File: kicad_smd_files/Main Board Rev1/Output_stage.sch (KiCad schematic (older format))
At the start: 41 parts, among them J10 OUTPUT B, J9 OUTPUT A, Q3 DMN10H170SK3-13, Q4 DMP6180SK3-13, Q5 DMN10H170SK3-13, Q6 DMN10H170SK3-13, Q7 DMP6180SK3-13, Q8 DMN10H170SK3-13, U7 LM358N, U8 LTC1661

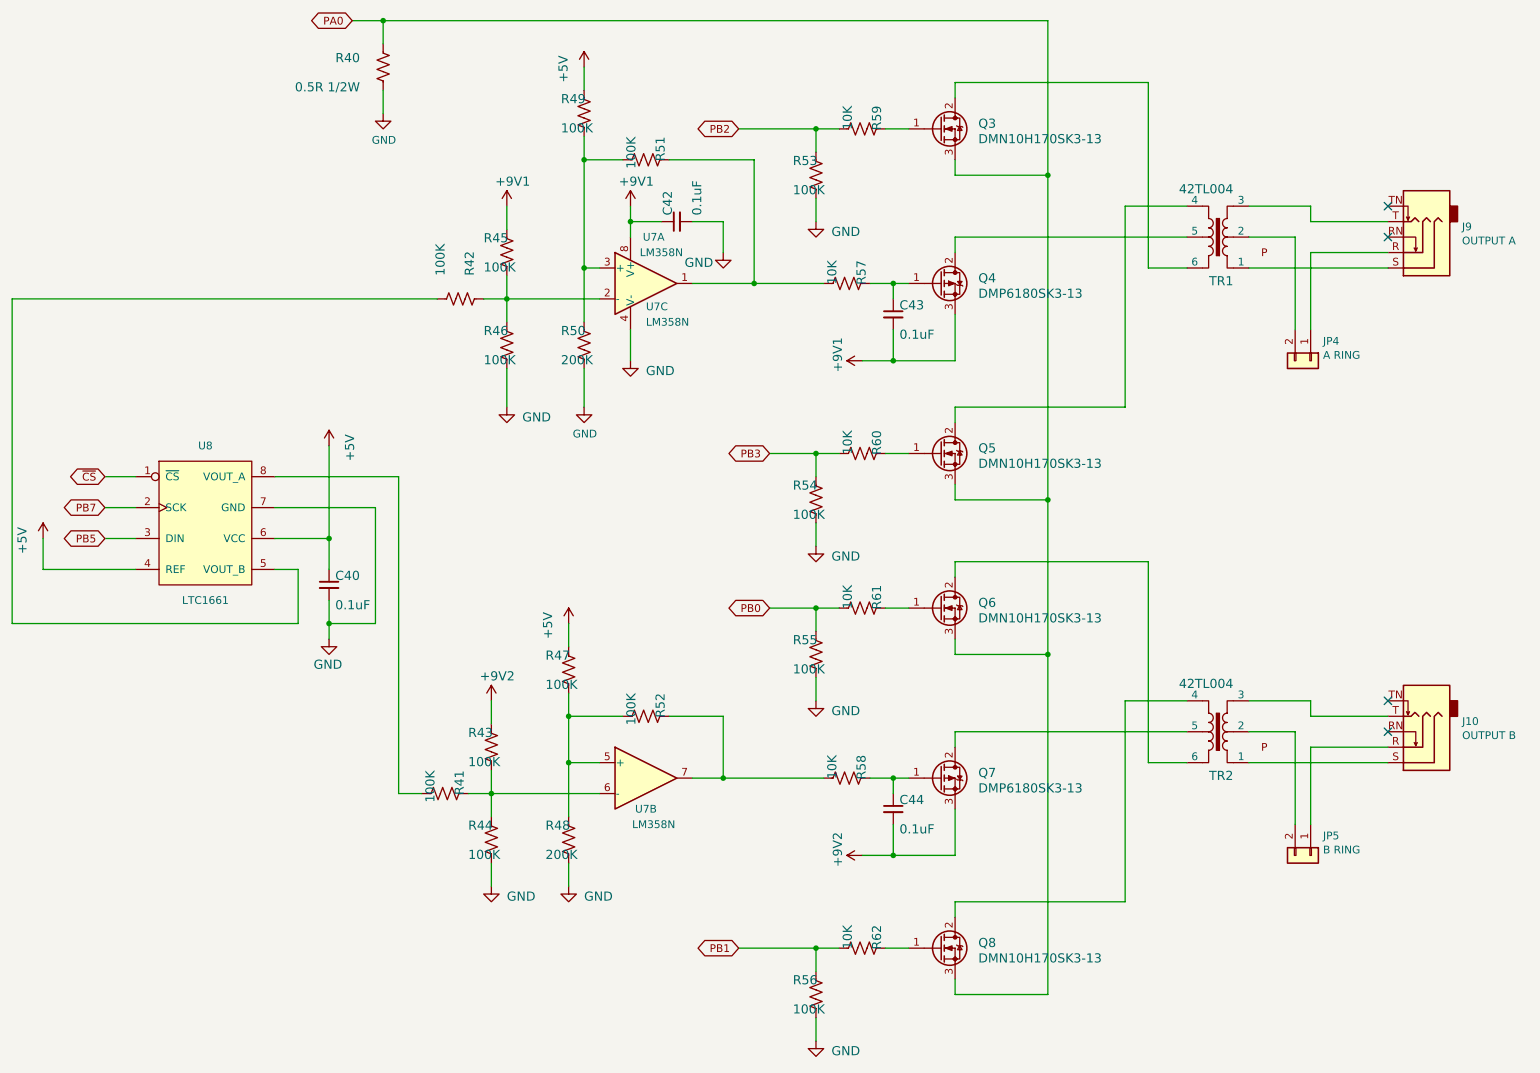
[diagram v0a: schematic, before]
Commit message: Firmware patch to support new LCD, more beefy power circuit for LiPo, added LiPo Balance and protection, fixed reversed op-amp comparitor pins
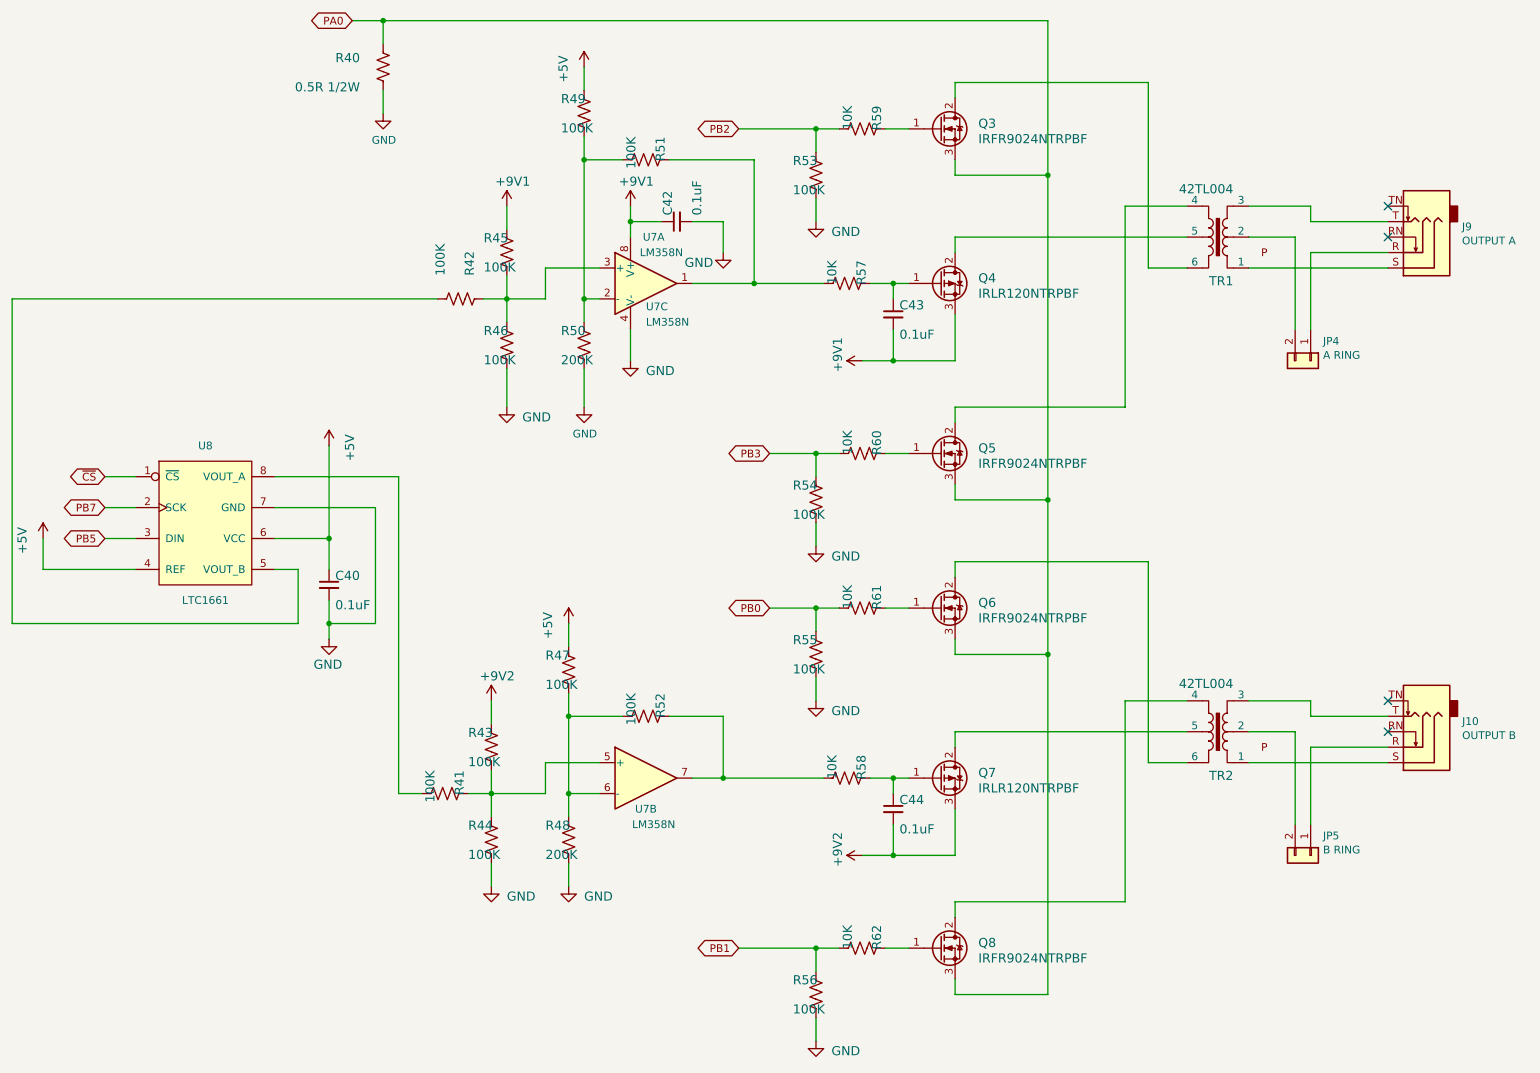
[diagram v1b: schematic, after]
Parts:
- Q3, Q5, Q6, Q8: value DMN10H170SK3-13 -> IRFR9024NTRPBF; Manufacturer_Name Diodes Incorporated -> Infineon; Manufacturer_Part_Number DMN10H170SK3-13 -> IRFR9024NTRPBF; Mouser Part Number 621-DMN10H170SK3-13 -> 942-IRFR9024NTRPBF
- Q4, Q7: value DMP6180SK3-13 -> IRLR120NTRPBF; Manufacturer_Name Diodes Incorporated -> Infineon; Manufacturer_Part_Number DMP6180SK3-13 -> IRLR120NTRPBF; Mouser Part Number 621-DMP6180SK3-13 -> 942-IRLR120NTRPBF
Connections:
- net at R47.2, R48.1, R52.2: now also U7.6 (-); no longer U7.5 (+)
- net at R41.1, R43.2, R44.1: now also U7.5 (+); no longer U7.6 (-)
- net at R49.2, R50.1, R51.2: now also U7.2 (-); no longer U7.3 (+)
- net at R42.1, R45.2, R46.1: now also U7.3 (+); no longer U7.2 (-)
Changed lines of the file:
@@
 	7400 2500 7400 2400
 Connection ~ 7400 2400
-Wire Wire Line
-	4900 2500 5500 2500
 Connection ~ 4900 2500
 Wire Wire Line
@@
 	7400 5700 7400 5600
 Connection ~ 7400 5600
-Wire Wire Line
-	5500 5700 4800 5700
 Connection ~ 4800 5700
 Text GLabel 2300 3850 0    50   BiDi ~ 0
@@
 PA0
 Connection ~ 4100 700
-Wire Wire Line
-	5400 1600 5400 2300
-Wire Wire Line
-	5400 2300 5500 2300
-Connection ~ 5400 2300
-Connection ~ 5400 1600
-Wire Wire Line
-	5300 5500 5300 5200
-Wire Wire Line
-	5500 5500 5300 5500
-Connection ~ 5300 5200
-Connection ~ 5300 5500
 Text GLabel 2300 4050 0    50   BiDi ~ 0
 PB5
@@
 AR Path="/5CB41D9F/4F009C7F" Ref="Q3"  Part="1"
 F 0 "Q3" H 7950 1400 59  0000 L BNN
-F 1 "DMN10H170SK3-13" H 7950 1300 59  0000 L BNN
+F 1 "IRFR9024NTRPBF" H 7950 1300 59  0000 L BNN
 F 2 "Package_TO_SOT_SMD:TO-252-2" H 7700 1400 50  0001 C CNN
-F 3 "https://www.mouser.com/datasheet/2/115/DMN10H170SK3-1594697.pdf" H 7700 1400 50  0001 C CNN
-F 4 "Diodes Incorporated" H 7700 1400 50  0001 C CNN "Manufacturer_Name"
-F 5 "DMN10H170SK3-13" H 7700 1400 50  0001 C CNN "Manufacturer_Part_Number"
-F 6 "621-DMN10H170SK3-13" H 7700 1400 50  0001 C CNN "Mouser Part Number"
+F 3 "https://www.mouser.com/datasheet/2/196/irfr9024npbf-1228513.pdf" H 7700 1400 50  0001 C CNN
+F 4 "Infineon" H 7700 1400 50  0001 C CNN "Manufacturer_Name"
+F 5 "IRFR9024NTRPBF" H 7700 1400 50  0001 C CNN "Manufacturer_Part_Number"
+F 6 "942-IRFR9024NTRPBF" H 7700 1400 50  0001 C CNN "Mouser Part Number"
 	1    7700 1400
 	1    0    0    -1
@@
 AR Path="/5CB41D9F/91F1D459" Ref="Q5"  Part="1"
 F 0 "Q5" H 7950 3500 59  0000 L BNN
-F 1 "DMN10H170SK3-13" H 7950 3400 59  0000 L BNN
+F 1 "IRFR9024NTRPBF" H 7950 3400 59  0000 L BNN
 F 2 "Package_TO_SOT_SMD:TO-252-2" H 7700 3500 50  0001 C CNN
-F 3 "https://www.mouser.com/datasheet/2/115/DMN10H170SK3-1594697.pdf" H 7700 3500 50  0001 C CNN
-F 4 "Diodes Incorporated" H 7700 3500 50  0001 C CNN "Manufacturer_Name"
-F 5 "DMN10H170SK3-13" H 7700 3500 50  0001 C CNN "Manufacturer_Part_Number"
-F 6 "621-DMN10H170SK3-13" H 7700 3500 50  0001 C CNN "Mouser Part Number"
+F 3 "https://www.mouser.com/datasheet/2/196/irfr9024npbf-1228513.pdf" H 7700 3500 50  0001 C CNN
+F 4 "Infineon" H 7700 3500 50  0001 C CNN "Manufacturer_Name"
+F 5 "IRFR9024NTRPBF" H 7700 3500 50  0001 C CNN "Manufacturer_Part_Number"
+F 6 "942-IRFR9024NTRPBF" H 7700 3500 50  0001 C CNN "Mouser Part Number"
 	1    7700 3500
 	1    0    0    -1
@@
 AR Path="/5CB41D9F/E26DE37C" Ref="Q4"  Part="1"
 F 0 "Q4" H 7950 2400 59  0000 L BNN
-F 1 "DMP6180SK3-13" H 7950 2300 59  0000 L BNN
+F 1 "IRLR120NTRPBF" H 7950 2300 59  0000 L BNN
 F 2 "Package_TO_SOT_SMD:TO-252-2" H 7700 2400 50  0001 C CNN
-F 3 "https://www.mouser.com/datasheet/2/115/DMP6180SK3-247239.pdf" H 7700 2400 50  0001 C CNN
-F 4 "Diodes Incorporated" H 7700 2400 50  0001 C CNN "Manufacturer_Name"
-F 5 "DMP6180SK3-13" H 7700 2400 50  0001 C CNN "Manufacturer_Part_Number"
-F 6 "621-DMP6180SK3-13" H 7700 2400 50  0001 C CNN "Mouser Part Number"
+F 3 "https://www.mouser.com/datasheet/2/196/irlr120npbf-1228003.pdf" H 7700 2400 50  0001 C CNN
+F 4 "Infineon" H 7700 2400 50  0001 C CNN "Manufacturer_Name"
+F 5 "IRLR120NTRPBF" H 7700 2400 50  0001 C CNN "Manufacturer_Part_Number"
+F 6 "942-IRLR120NTRPBF" H 7700 2400 50  0001 C CNN "Mouser Part Number"
 	1    7700 2400
 	1    0    0    -1
@@
 AR Path="/5CB41D9F/4FF9B51F" Ref="Q6"  Part="1"
 F 0 "Q6" H 7950 4500 59  0000 L BNN
-F 1 "DMN10H170SK3-13" H 7950 4400 59  0000 L BNN
+F 1 "IRFR9024NTRPBF" H 7950 4400 59  0000 L BNN
 F 2 "Package_TO_SOT_SMD:TO-252-2" H 7700 4500 50  0001 C CNN
-F 3 "https://www.mouser.com/datasheet/2/115/DMN10H170SK3-1594697.pdf" H 7700 4500 50  0001 C CNN
-F 4 "Diodes Incorporated" H 7700 4500 50  0001 C CNN "Manufacturer_Name"
-F 5 "DMN10H170SK3-13" H 7700 4500 50  0001 C CNN "Manufacturer_Part_Number"
-F 6 "621-DMN10H170SK3-13" H 7700 4500 50  0001 C CNN "Mouser Part Number"
+F 3 "https://www.mouser.com/datasheet/2/196/irfr9024npbf-1228513.pdf" H 7700 4500 50  0001 C CNN
+F 4 "Infineon" H 7700 4500 50  0001 C CNN "Manufacturer_Name"
+F 5 "IRFR9024NTRPBF" H 7700 4500 50  0001 C CNN "Manufacturer_Part_Number"
+F 6 "942-IRFR9024NTRPBF" H 7700 4500 50  0001 C CNN "Mouser Part Number"
 	1    7700 4500
 	1    0    0    -1
@@
 AR Path="/5CB41D9F/CE8964FE" Ref="Q8"  Part="1"
 F 0 "Q8" H 7950 6700 59  0000 L BNN
-F 1 "DMN10H170SK3-13" H 7950 6600 59  0000 L BNN
+F 1 "IRFR9024NTRPBF" H 7950 6600 59  0000 L BNN
 F 2 "Package_TO_SOT_SMD:TO-252-2" H 7700 6700 50  0001 C CNN
-F 3 "https://www.mouser.com/datasheet/2/115/DMN10H170SK3-1594697.pdf" H 7700 6700 50  0001 C CNN
-F 4 "Diodes Incorporated" H 7700 6700 50  0001 C CNN "Manufacturer_Name"
-F 5 "DMN10H170SK3-13" H 7700 6700 50  0001 C CNN "Manufacturer_Part_Number"
-F 6 "621-DMN10H170SK3-13" H 7700 6700 50  0001 C CNN "Mouser Part Number"
+F 3 "https://www.mouser.com/datasheet/2/196/irfr9024npbf-1228513.pdf" H 7700 6700 50  0001 C CNN
+F 4 "Infineon" H 7700 6700 50  0001 C CNN "Manufacturer_Name"
+F 5 "IRFR9024NTRPBF" H 7700 6700 50  0001 C CNN "Manufacturer_Part_Number"
+F 6 "942-IRFR9024NTRPBF" H 7700 6700 50  0001 C CNN "Mouser Part Number"
 	1    7700 6700
 	1    0    0    -1
@@
 AR Path="/5CB41D9F/EF13FC82" Ref="Q7"  Part="1"
 F 0 "Q7" H 7950 5600 59  0000 L BNN
-F 1 "DMP6180SK3-13" H 7950 5500 59  0000 L BNN
+F 1 "IRLR120NTRPBF" H 7950 5500 59  0000 L BNN
 F 2 "Package_TO_SOT_SMD:TO-252-2" H 7700 5600 50  0001 C CNN
-F 3 "https://www.mouser.com/datasheet/2/115/DMP6180SK3-247239.pdf" H 7700 5600 50  0001 C CNN
-F 4 "Diodes Incorporated" H 7700 5600 50  0001 C CNN "Manufacturer_Name"
-F 5 "DMP6180SK3-13" H 7700 5600 50  0001 C CNN "Manufacturer_Part_Number"
-F 6 "621-DMP6180SK3-13" H 7700 5600 50  0001 C CNN "Mouser Part Number"
+F 3 "https://www.mouser.com/datasheet/2/196/irlr120npbf-1228003.pdf" H 7700 5600 50  0001 C CNN
+F 4 "Infineon" H 7700 5600 50  0001 C CNN "Manufacturer_Name"
+F 5 "IRLR120NTRPBF" H 7700 5600 50  0001 C CNN "Manufacturer_Part_Number"
+F 6 "942-IRLR120NTRPBF" H 7700 5600 50  0001 C CNN "Mouser Part Number"
 	1    7700 5600
 	1    0    0    -1
@@
 	5300 5050 5300 5200
 Wire Wire Line
-	5300 5500 5300 5850
-Wire Wire Line
 	5300 6150 5300 6300
 Wire Wire Line
@@
 Wire Wire Line
 	5400 2950 5400 3200
-Wire Wire Line
-	5400 2300 5400 2650
 Wire Wire Line
 	4900 2500 4900 2650
@@
 Wire Wire Line
 	7800 1100 9050 1100
+Wire Wire Line
+	4900 2500 5150 2500
+Wire Wire Line
+	5150 2500 5150 2300
+Wire Wire Line
+	5150 2300 5500 2300
+Wire Wire Line
+	5500 2500 5400 2500
+Wire Wire Line
+	5400 2500 5400 1600
+Connection ~ 5400 1600
+Wire Wire Line
+	5400 2500 5400 2650
+Connection ~ 5400 2500
+Wire Wire Line
+	4800 5700 5150 5700
+Wire Wire Line
+	5150 5700 5150 5500
+Wire Wire Line
+	5150 5500 5500 5500
+Wire Wire Line
+	5300 5200 5300 5700
+Wire Wire Line
+	5300 5700 5500 5700
+Connection ~ 5300 5200
+Wire Wire Line
+	5300 5700 5300 5850
+Connection ~ 5300 5700
 $EndSCHEMATC
